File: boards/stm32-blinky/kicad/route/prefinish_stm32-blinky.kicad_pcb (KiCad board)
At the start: 2 copper layers, 50 x 40 mm, 20 parts, among them J1 1x2 2.54mm male THT, J2 1x4 2.54mm male THT, U1 STM32F103C8T6, U2 AMS1117-3.3, Y1 8MHz 20pF

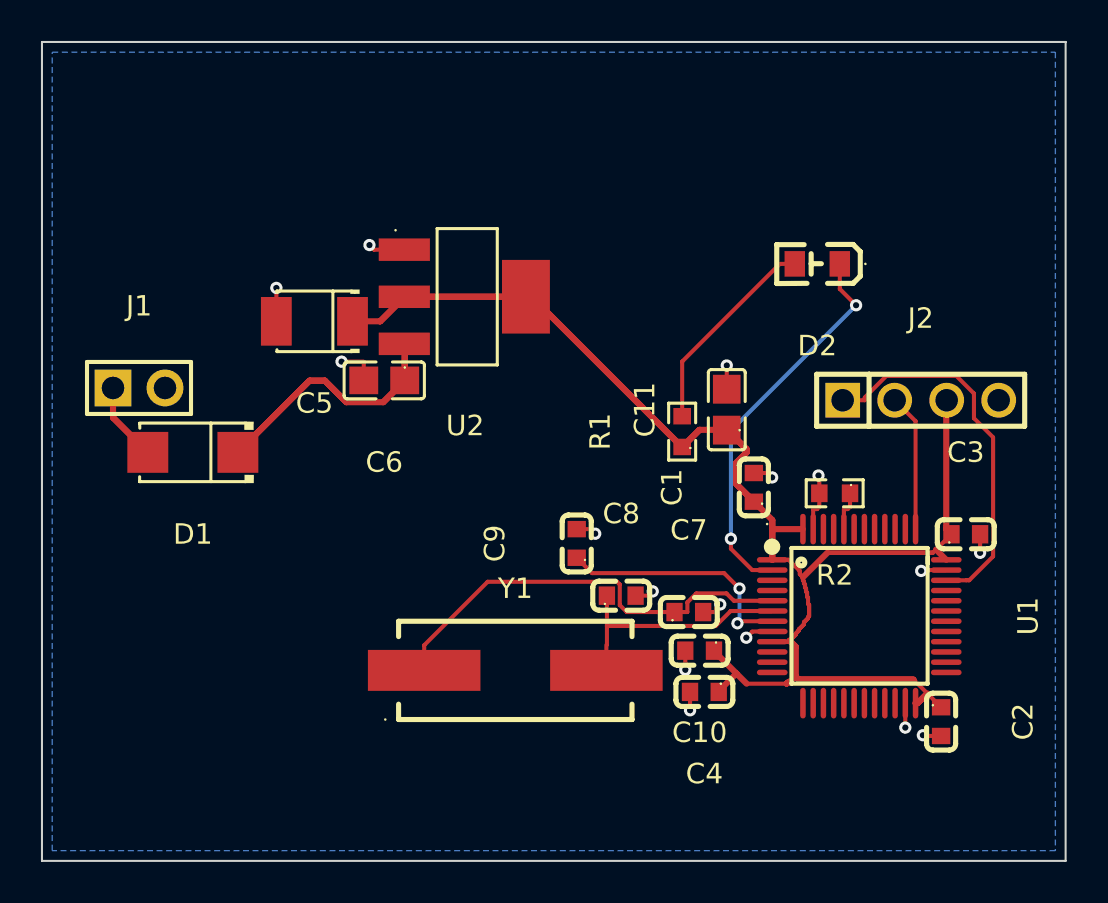
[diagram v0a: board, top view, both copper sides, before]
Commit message: ai-ee stm32-blinky: drc_routed pass (attempt 2, post P7->P6 relief)
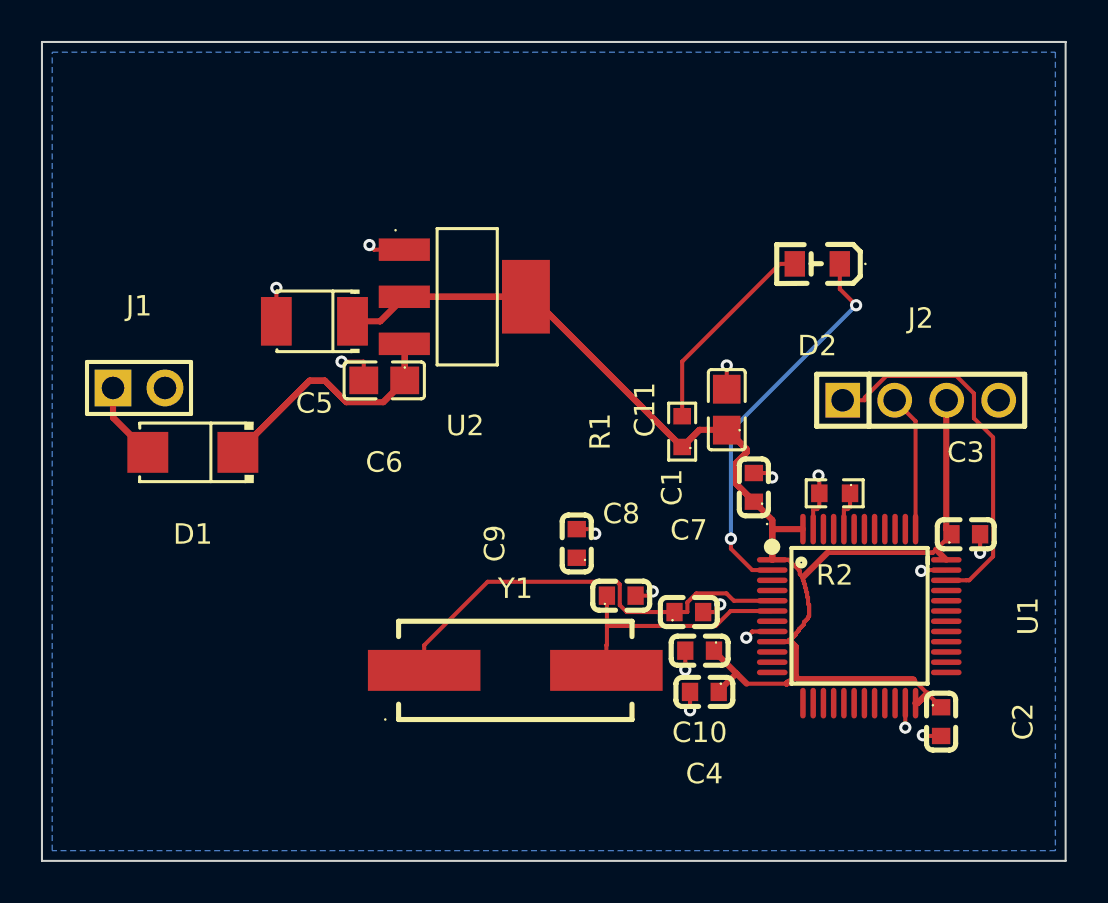
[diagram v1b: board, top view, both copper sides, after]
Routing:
- net /NRST: track 11.9 -> 0.00 mm, vias 2 -> 0
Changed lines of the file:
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@@
+	)
+	(segment
+		(start 27.1 23.7)
+		(end 27.08 23.7)
+		(width 0.3)
+		(layer "F.Cu")
+		(net "+5V")
 	)
 	(segment
@@
 	)
 	(segment
+		(start 27.1 23.7)
+		(end 27.08 23.7)
+		(width 0.3)
+		(layer "F.Cu")
+		(net "+5V")
+	)
+	(segment
 		(start 27.1 25.5)
 		(end 27.1 23.7)
@@
 	)
 	(segment
+		(start 42.85 27.9)
+		(end 42.8286 27.917)
+		(width 0.3)
+		(layer "F.Cu")
+		(net "+3V3")
+	)
+	(segment
+		(start 24.5489 22.6)
+		(end 24.55 22.6)
+		(width 0.254)
+		(layer "F.Cu")
+		(net "+3V3")
+	)
+	(segment
+		(start 42.2041 38.687)
+		(end 42.2 38.6911)
+		(width 0.254)
+		(layer "F.Cu")
+		(net "+3V3")
+	)
+	(segment
 		(start 52.15 41.25)
 		(end 52.05 41.25)
@@
 	)
 	(segment
+		(start 53.8011 33.0011)
+		(end 53.8 33)
+		(width 0.254)
+		(layer "F.Cu")
+		(net "+3V3")
+	)
+	(segment
 		(start 33 21.4)
 		(end 33.3 21.4)
@@
 	)
 	(segment
+		(start 42.2 38.6911)
+		(end 42.2 38.7)
+		(width 0.254)
+		(layer "F.Cu")
+		(net "+3V3")
+	)
+	(segment
 		(start 40.65 28.75)
 		(end 33.3 21.4)
@@
 	)
 	(segment
+		(start 33 21.4)
+		(end 33.02 21.4)
+		(width 0.3)
+		(layer "F.Cu")
+		(net "+3V3")
+	)
+	(segment
 		(start 51.95 40.1)
 		(end 53.3 41.45)
@@
 	)
 	(segment
+		(start 53.8028 33.0011)
+		(end 53.8011 33.0011)
+		(width 0.254)
+		(layer "F.Cu")
+		(net "+3V3")
+	)
+	(segment
 		(start 46.65 35.45)
 		(end 46.65 35.6)
@@
 	)
 	(segment
+		(start 46.2 37.85)
+		(end 46.2 37.9)
+		(width 0.2)
+		(layer "F.Cu")
+		(net "+3V3")
+	)
+	(segment
 		(start 43.8 28.85)
 		(end 43.8 29)
@@
 	)
 	(segment
+		(start 46.2 37.85)
+		(end 46.2 37.9)
+		(width 0.2)
+		(layer "F.Cu")
+		(net "+3V3")
+	)
+	(segment
 		(start 46.55 35.1)
 		(end 46.55 35.25)
@@
 	)
 	(segment
+		(start 44.0713 37.75)
+		(end 44.0713 37.7647)
+		(width 0.2)
+		(layer "F.Cu")
+		(net "GND")
+	)
+	(segment
 		(start 47.35 31.6607)
 		(end 47.2394 31.7713)
@@
 	)
 	(segment
+		(start 25.0857 24.569)
+		(end 25.0983 24.5816)
+		(width 0.2)
+		(layer "F.Cu")
+		(net "GND")
+	)
+	(segment
 		(start 20.8289 22.6)
 		(end 20.8289 20.9678)
@@
 	)
 	(segment
-		(start 36.25 34.9)
-		(end 42.7 34.9)
-		(width 0.2)
-		(layer "F.Cu")
-		(net "/NRST")
-	)
-	(segment
-		(start 43.45 37.25)
-		(end 45.05 37.25)
-		(width 0.2)
-		(layer "F.Cu")
-		(net "/NRST")
-	)
-	(segment
-		(start 35.5 34.15)
-		(end 36.25 34.9)
-		(width 0.2)
-		(layer "F.Cu")
-		(net "/NRST")
-	)
-	(segment
-		(start 43.35 37.35)
-		(end 43.45 37.25)
-		(width 0.2)
-		(layer "F.Cu")
-		(net "/NRST")
-	)
-	(segment
-		(start 42.7 34.9)
-		(end 43.45 35.65)
-		(width 0.2)
-		(layer "F.Cu")
-		(net "/NRST")
-	)
-	(via
-		(at 43.45 35.65)
-		(size 0.6)
-		(drill 0.3)
-		(layers "F.Cu" "B.Cu")
-		(tenting
-			(front yes)
-			(back yes)
-		)
-		(net "/NRST")
-	)
-	(via
-		(at 43.35 37.35)
-		(size 0.6)
-		(drill 0.3)
-		(layers "F.Cu" "B.Cu")
-		(tenting
-			(front yes)
-			(back yes)
-		)
-		(net "/NRST")
-	)
-	(segment
-		(start 43.45 35.65)
-		(end 43.45 37.25)
-		(width 0.2)
-		(layer "B.Cu")
-		(net "/NRST")
-	)
-	(segment
 		(start 48.7394 31.7713)
 		(end 48.85 31.6607)
@@
 		(width 0.2)
 		(layer "F.Cu")
+		(net "/OSC_OUT")
+	)
+	(segment
+		(start 36.95 38.4213)
+		(end 36.9748 38.3965)
+		(width 0.2)
+		(layer "F.Cu")
